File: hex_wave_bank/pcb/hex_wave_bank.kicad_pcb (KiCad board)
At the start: 2 copper layers, 19 x 110 mm, 101 parts, among them J101 Conn_02x05_Odd_Even, J201 AudioJack2_SwitchT, J301 AudioJack2_SwitchT, J401 AudioJack2_SwitchT, J501 AudioJack2_SwitchT, J601 AudioJack2_SwitchT, J701 AudioJack2_SwitchT, U201 TL071HDBV, U301 TL071HDBV, U401 TL071HDBV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

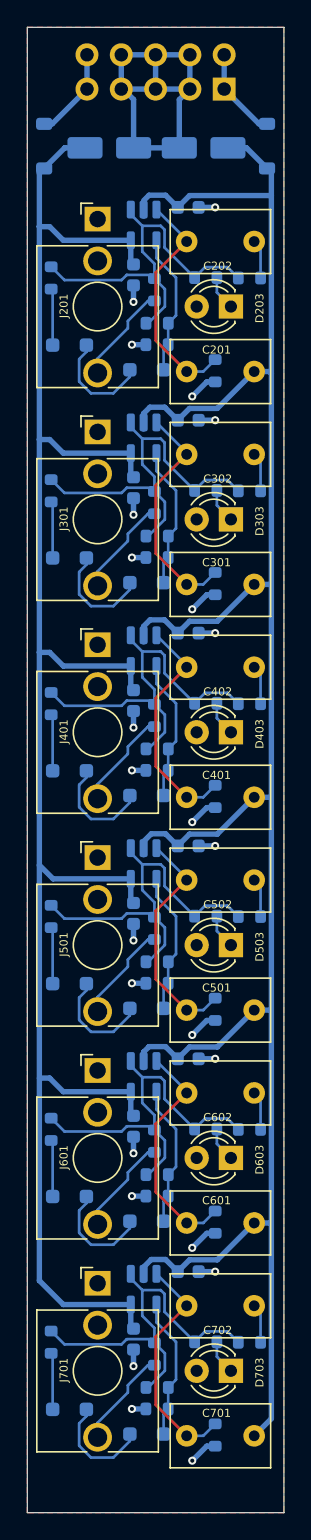
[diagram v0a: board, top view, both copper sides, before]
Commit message: Add another ground plane, add capacitor values
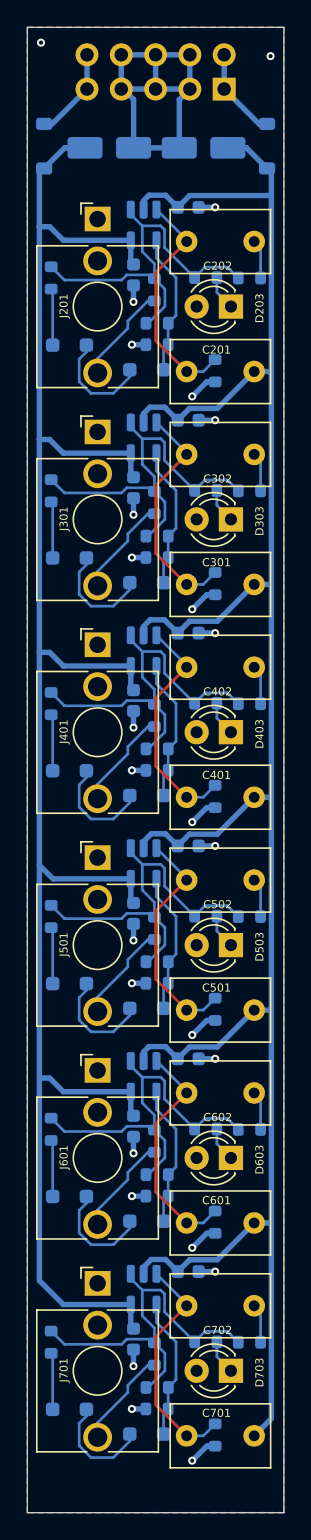
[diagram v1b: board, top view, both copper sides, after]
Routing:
- net GND: vias 24 -> 26
- added copper zone on B.Cu, net GND
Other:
- board text added: "Hex Wave Bank v1.2 www.birchavenue.org"
- board text removed: "Hex Wave Bank v1.1 www.birchavenue.org"
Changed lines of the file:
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@@
 		)
 	)
-	(gr_text "Hex Wave Bank v1.1\nwww.birchavenue.org"
+	(gr_text "Hex Wave Bank v1.2\nwww.birchavenue.org"
 		(at 149.4605 142.6805 0)
 		(layer "B.SilkS")
@@
 	)
 	(via
+		(at 150.5 35.5)
+		(size 0.6)
+		(drill 0.3)
+		(layers "F.Cu" "B.Cu")
+		(free yes)
+		(net 1)
+	)
+	(via
 		(at 140.35 69.464)
 		(size 0.6)
@@
 		(net 1)
 	)
+	(via
+		(at 133.5 34.5)
+		(size 0.6)
+		(drill 0.3)
+		(layers "F.Cu" "B.Cu")
+		(free yes)
+		(net 1)
+	)
 	(segment
 		(start 140.35 52.475)
@@
 			)
 		)
+	)
+	(zone
+		(net 1)
+		(net_name "GND")
+		(layer "B.Cu")
+		(hatch edge 0.5)
+		(priority 1)
+		(connect_pads
+			(clearance 0.5)
+		)
+		(min_thickness 0.25)
+		(filled_areas_thickness no)
+		(fill yes
+			(thermal_gap 0.5)
+			(thermal_bridge_width 0.5)
+			(island_removal_mode 2)
+			(island_area_min 10)
+		)
+		(polygon
+			(pts
+				(xy 132.49 33.37) (xy 151.49 33.37) (xy 151.49 143.36) (xy 132.49 143.37)
+			)
+		)
